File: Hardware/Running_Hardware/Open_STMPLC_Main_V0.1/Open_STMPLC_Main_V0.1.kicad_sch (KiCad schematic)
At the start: 0 parts

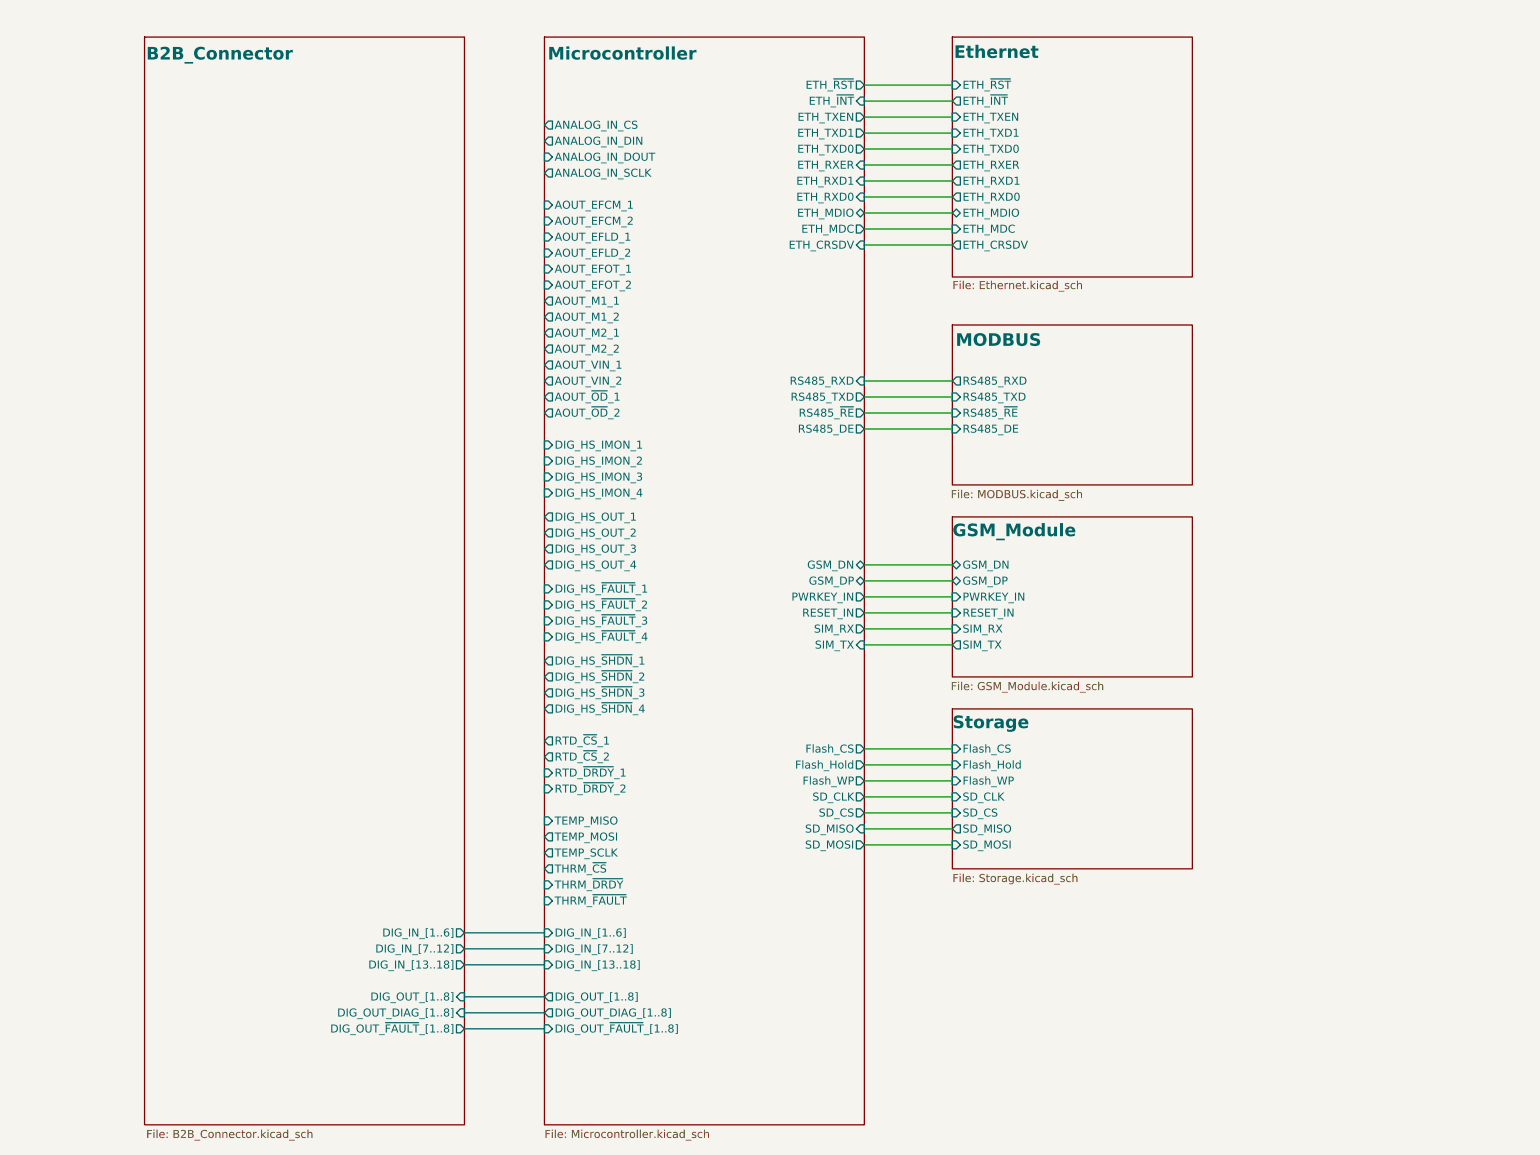
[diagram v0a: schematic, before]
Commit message: Pin mapping IO connector
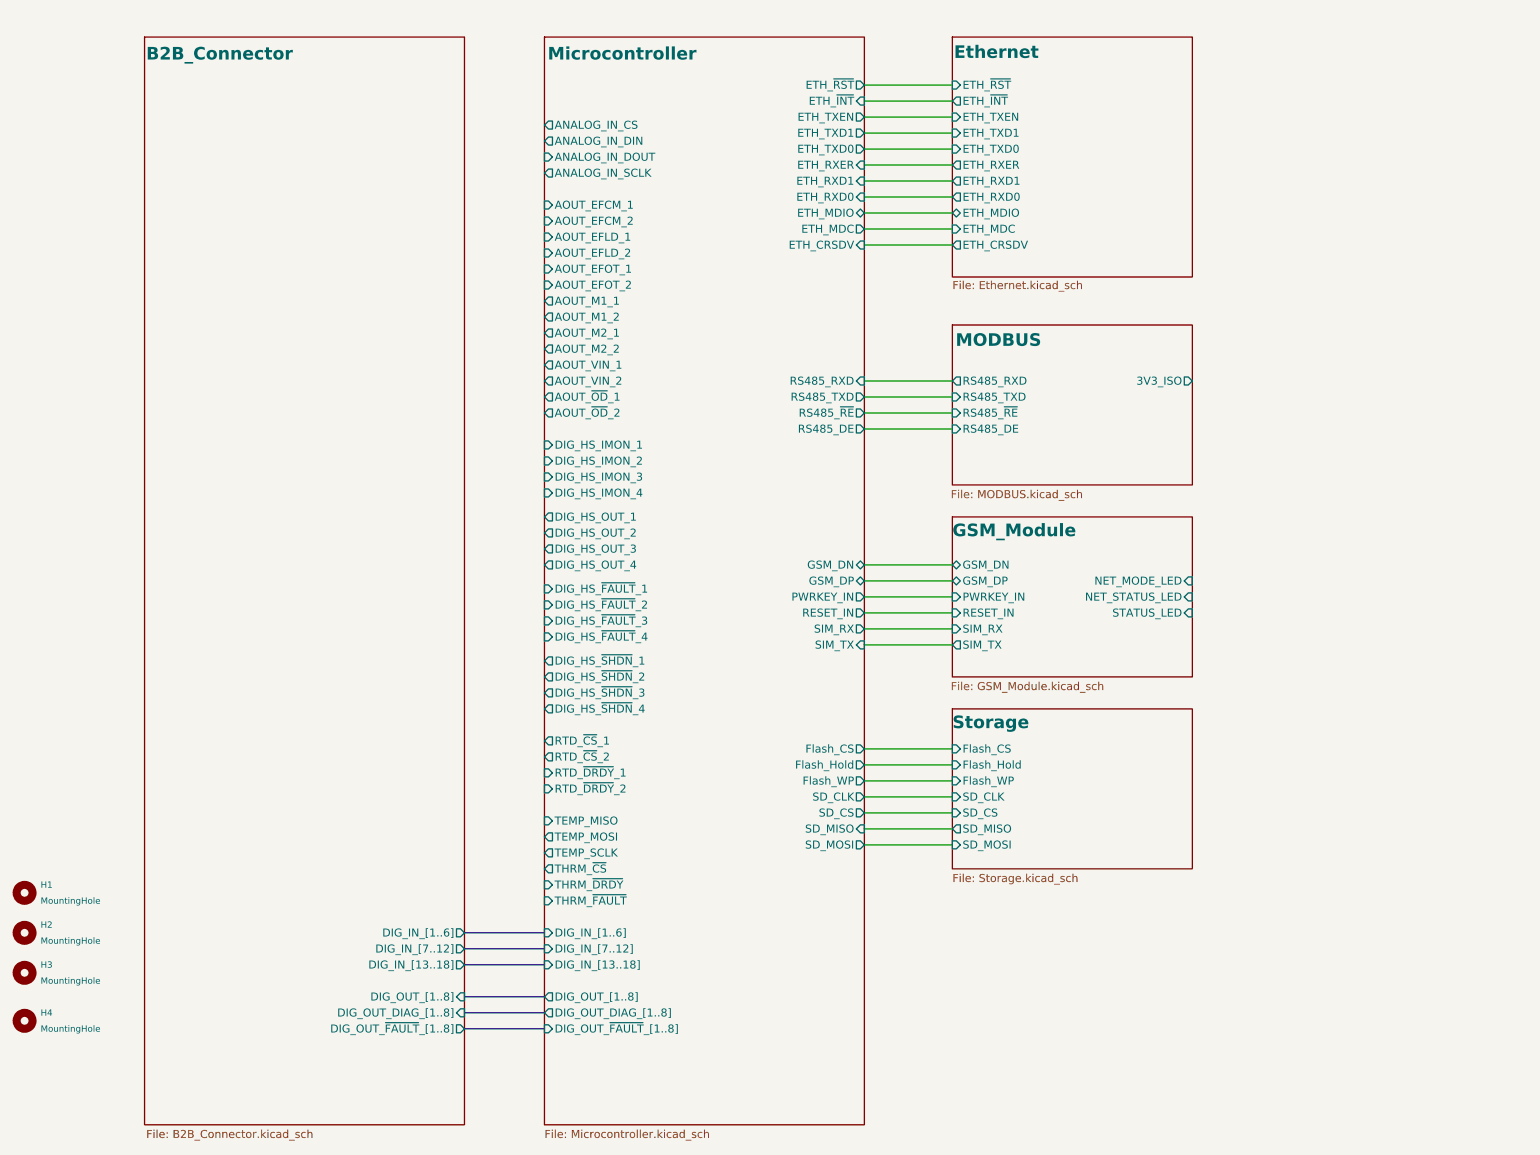
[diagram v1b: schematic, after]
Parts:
- added H1, H2, H3, H4: MountingHole, MountingHole:MountingHole_3.2mm_M3, symbol Mechanical:MountingHole
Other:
- sheet GSM_Module ports: added NET_MODE_LED, NET_STATUS_LED, STATUS_LED; removed none
- sheet MODBUS ports: added 3V3_ISO; removed none

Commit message: Main PCB changes
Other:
- sheet B2B_Connector ports: added 3V3_ISO, AB+, AB-, ANALOG_IN_CS, ANALOG_IN_DIN, ANALOG_IN_DOUT, ANALOG_IN_ERROR, ANALOG_IN_SCLK, AOUT_EFCM_1, AOUT_EFCM_2, AOUT_EFLD_1, AOUT_EFLD_2, AOUT_EFOT_1, AOUT_EFOT_2, AOUT_M1_1, AOUT_M1_2, AOUT_M2_1, AOUT_M2_2, AOUT_VIN_1, AOUT_VIN_2, AOUT_~{OD}_1, AOUT_~{OD}_2, DIG_HS_IMON_1, DIG_HS_IMON_2, DIG_HS_IMON_3, DIG_HS_IMON_4, DIG_HS_OUT_1, DIG_HS_OUT_2, DIG_HS_OUT_3, DIG_HS_OUT_4, DIG_HS_~{FAULT}_1, DIG_HS_~{FAULT}_2, DIG_HS_~{FAULT}_3, DIG_HS_~{FAULT}_4, DIG_HS_~{SHDN}_1, DIG_HS_~{SHDN}_2, DIG_HS_~{SHDN}_3, DIG_HS_~{SHDN}_4, GSM_STATUS_LED, NET_MODE_LED, NET_STATUS_LED, RTD_~{CS}_1, RTD_~{CS}_2, RTD_~{DRDY}_1, RTD_~{DRDY}_2, TEMP_MISO, TEMP_MOSI, TEMP_SCLK, THRM_~{CS}, THRM_~{DRDY}, THRM_~{FAULT}, YZ+, YZ-; removed none
- sheet GSM_Module ports: added GSM_STATUS_LED; removed STATUS_LED
- sheet MODBUS ports: added AB+, AB-, YZ+, YZ-; removed none
- sheet Microcontroller ports: added ANALOG_IN_ERROR; removed none
- moved on the sheet: H1, H2, H3, H4

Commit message: Component placement main pcb
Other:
- sheet Ethernet ports: added ETH_REFCLKO; removed ETH_~{INT}
- sheet Microcontroller ports: added ETH_REFCLKO, Flash_CLK, Flash_MISO, Flash_MOSI, SD_CMD, SD_DAT0, SD_DAT1, SD_DAT2, SD_DAT3, SD_DET; removed ETH_~{INT}, SD_CS, SD_MISO, SD_MOSI
- sheet Storage ports: added Flash_CLK, Flash_MISO, Flash_MOSI, SD_CMD, SD_DAT0, SD_DAT1, SD_DAT2, SD_DAT3, SD_DET; removed SD_CS, SD_MISO, SD_MOSI

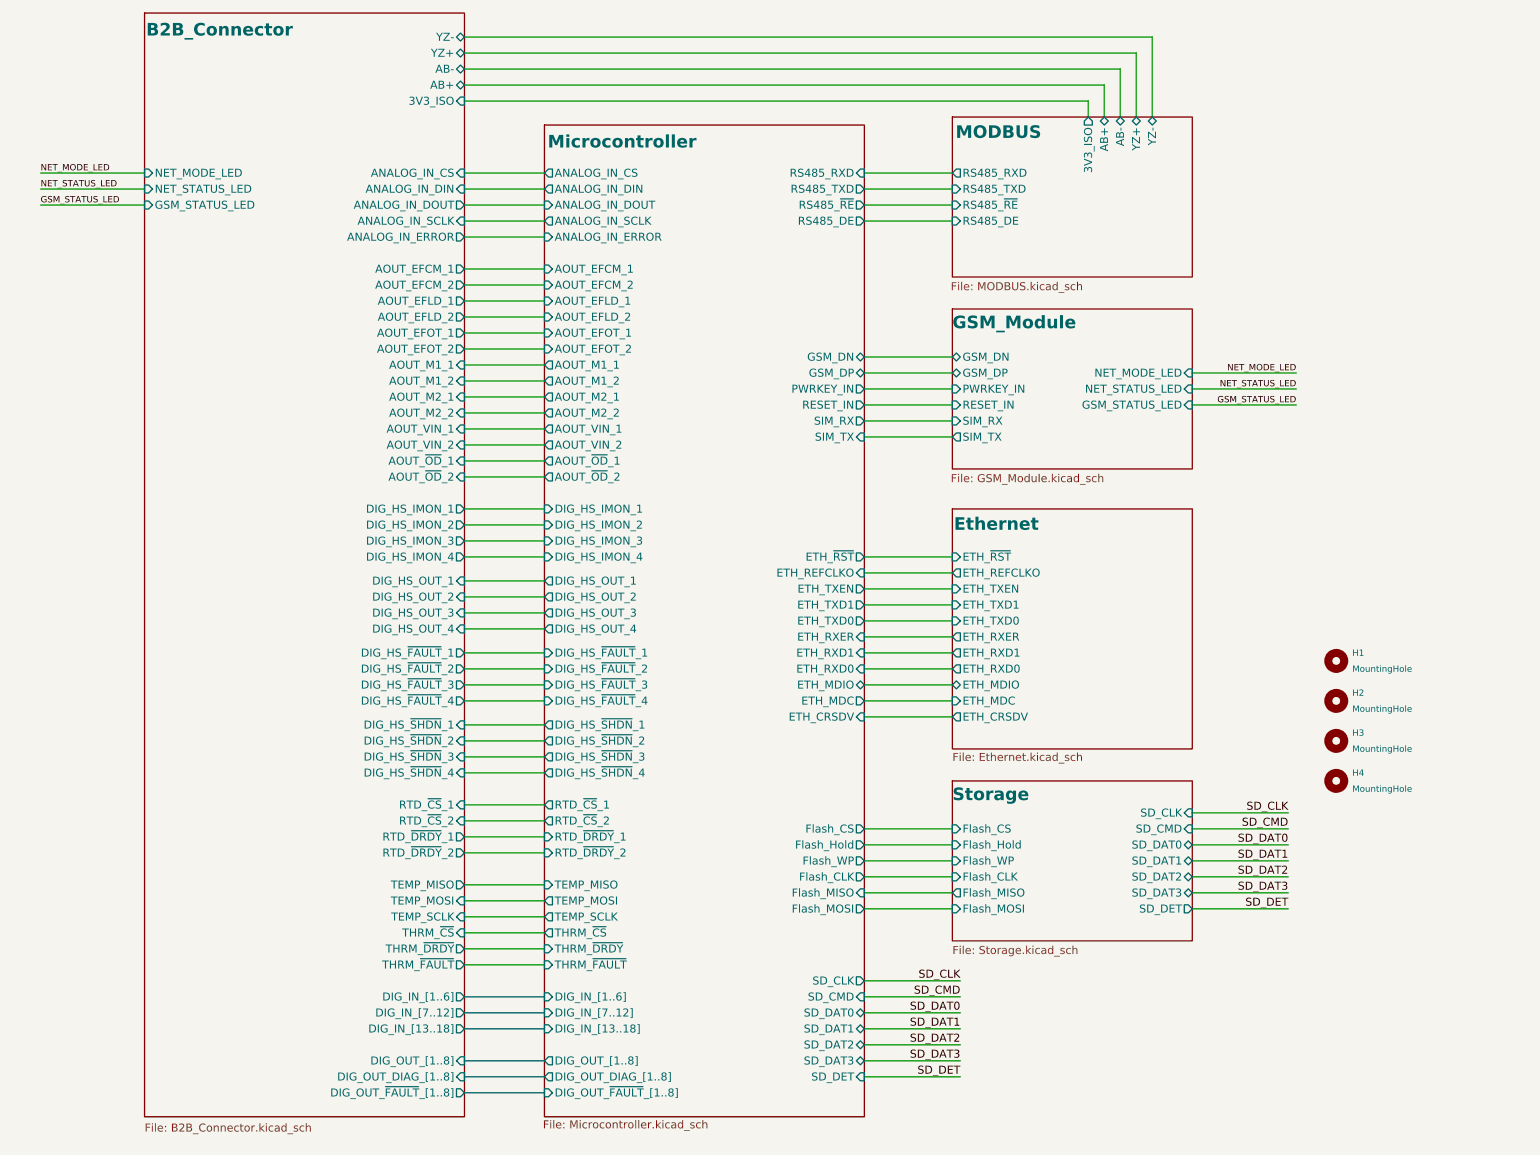
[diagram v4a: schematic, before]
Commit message: Layer stack up main PCB and pin mapping
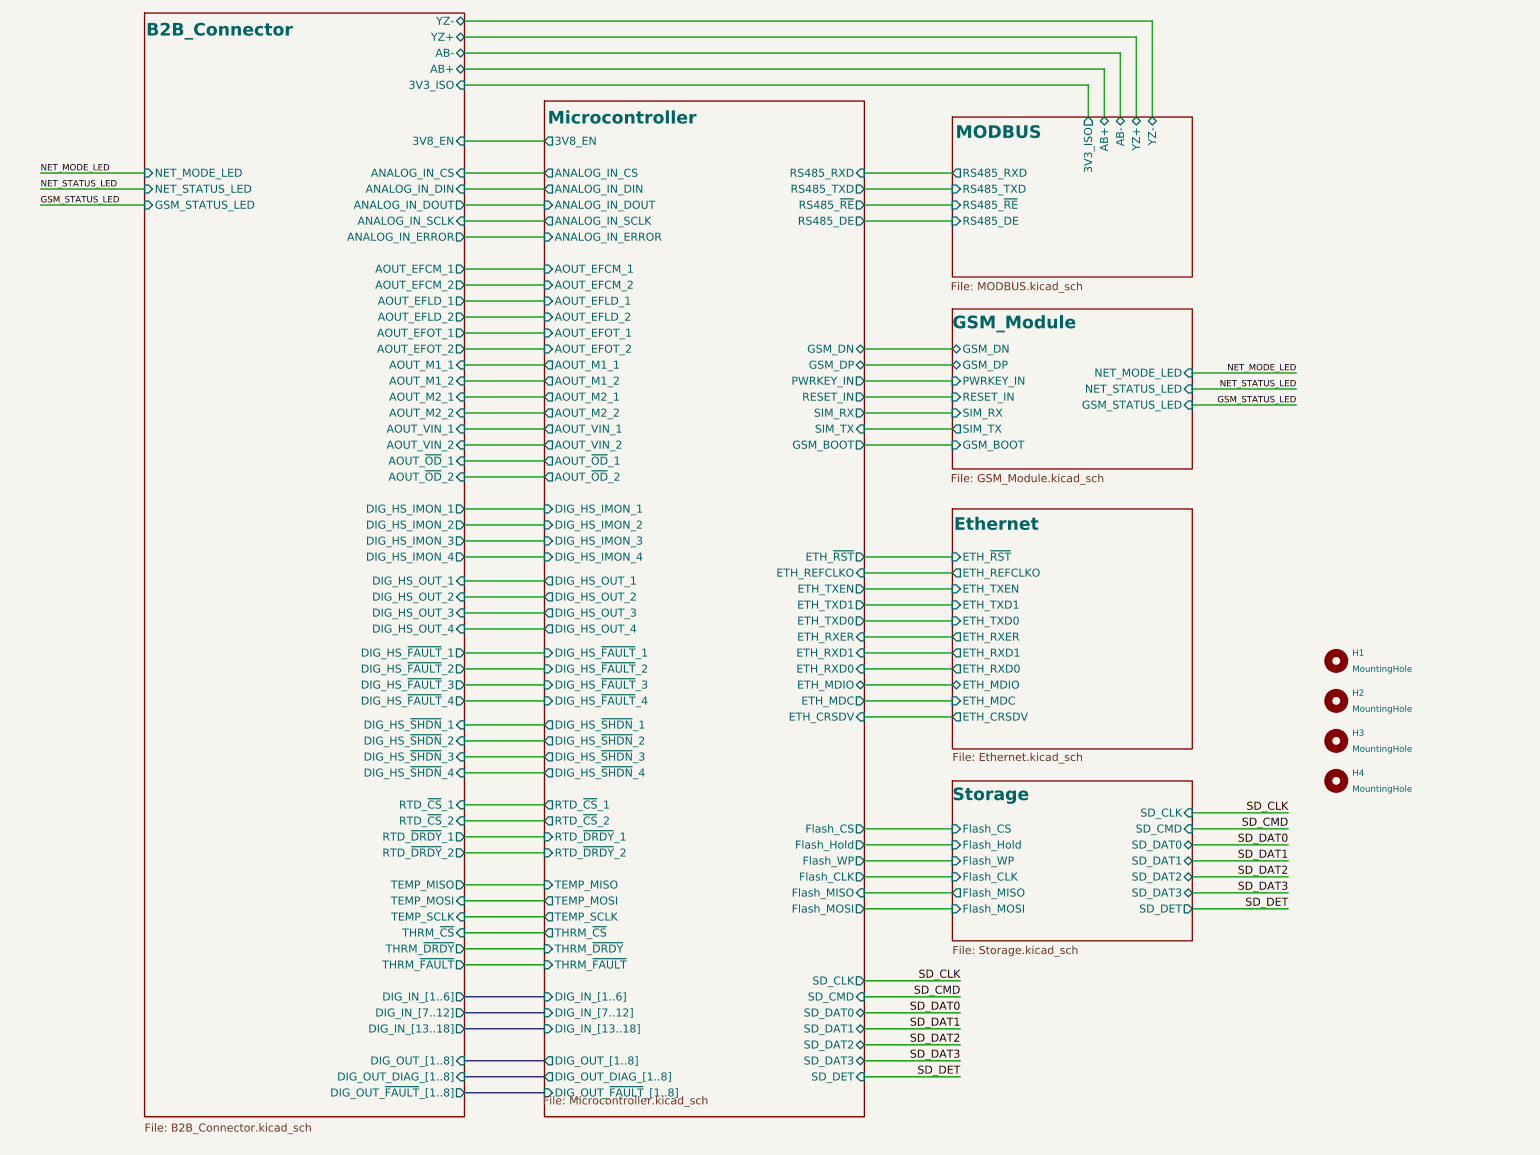
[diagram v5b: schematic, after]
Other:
- sheet B2B_Connector ports: added 3V8_EN; removed none
- sheet GSM_Module ports: added GSM_BOOT; removed none
- sheet Microcontroller ports: added 3V8_EN, GSM_BOOT; removed none
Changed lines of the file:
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@@
 	(wire
 		(pts
+			(xy 95.25 34.29) (xy 107.95 34.29)
+		)
+		(stroke
+			(width 0)
+			(type default)
+		)
+	)
+	(wire
+		(pts
 			(xy 95.25 157.48) (xy 107.95 157.48)
 		)
@@
 	(wire
 		(pts
-			(xy 158.75 68.58) (xy 172.72 68.58)
+			(xy 158.75 67.31) (xy 172.72 67.31)
 		)
 		(stroke
@@
 	(wire
 		(pts
-			(xy 196.85 30.48) (xy 196.85 25.4)
+			(xy 196.85 30.48) (xy 196.85 22.86)
 		)
 		(stroke
@@
 	(wire
 		(pts
-			(xy 201.93 20.32) (xy 201.93 30.48)
+			(xy 201.93 17.78) (xy 201.93 30.48)
 		)
 		(stroke
@@
 	(wire
 		(pts
-			(xy 204.47 30.48) (xy 204.47 17.78)
+			(xy 204.47 30.48) (xy 204.47 15.24)
 		)
 		(stroke
@@
 	(wire
 		(pts
-			(xy 194.31 27.94) (xy 194.31 30.48)
+			(xy 194.31 25.4) (xy 194.31 30.48)
 		)
 		(stroke
@@
 	(wire
 		(pts
+			(xy 158.75 82.55) (xy 172.72 82.55)
+		)
+		(stroke
+			(width 0)
+			(type default)
+		)
+	)
+	(wire
+		(pts
 			(xy 95.25 132.08) (xy 107.95 132.08)
 		)
@@
 	(wire
 		(pts
-			(xy 158.75 78.74) (xy 172.72 78.74)
+			(xy 158.75 77.47) (xy 172.72 77.47)
 		)
 		(stroke
@@
 	(wire
 		(pts
-			(xy 95.25 20.32) (xy 201.93 20.32)
+			(xy 95.25 17.78) (xy 201.93 17.78)
 		)
 		(stroke
@@
 	(wire
 		(pts
-			(xy 95.25 17.78) (xy 204.47 17.78)
+			(xy 95.25 15.24) (xy 204.47 15.24)
 		)
 		(stroke
@@
 	(wire
 		(pts
-			(xy 158.75 71.12) (xy 172.72 71.12)
+			(xy 158.75 69.85) (xy 172.72 69.85)
 		)
 		(stroke
@@
 	(wire
 		(pts
-			(xy 158.75 73.66) (xy 172.72 73.66)
+			(xy 158.75 72.39) (xy 172.72 72.39)
 		)
 		(stroke
@@
 	(wire
 		(pts
-			(xy 158.75 81.28) (xy 172.72 81.28)
+			(xy 158.75 80.01) (xy 172.72 80.01)
 		)
 		(stroke
@@
 	(wire
 		(pts
-			(xy 196.85 25.4) (xy 95.25 25.4)
+			(xy 196.85 22.86) (xy 95.25 22.86)
 		)
 		(stroke
@@
 	(wire
 		(pts
-			(xy 199.39 30.48) (xy 199.39 22.86)
+			(xy 199.39 30.48) (xy 199.39 20.32)
 		)
 		(stroke
@@
 	(wire
 		(pts
-			(xy 95.25 22.86) (xy 199.39 22.86)
+			(xy 95.25 20.32) (xy 199.39 20.32)
 		)
 		(stroke
@@
 	(wire
 		(pts
-			(xy 158.75 76.2) (xy 172.72 76.2)
+			(xy 158.75 74.93) (xy 172.72 74.93)
 		)
 		(stroke
@@
 	(wire
 		(pts
-			(xy 95.25 27.94) (xy 194.31 27.94)
+			(xy 95.25 25.4) (xy 194.31 25.4)
 		)
 		(stroke
@@
 		)
 		(pin "3V3_ISO" input
-			(at 95.25 27.94 0)
+			(at 95.25 25.4 0)
 			(effects
 				(font
@@
 		)
 		(pin "AB+" bidirectional
-			(at 95.25 25.4 0)
+			(at 95.25 22.86 0)
 			(effects
 				(font
@@
 		)
 		(pin "AB-" bidirectional
-			(at 95.25 22.86 0)
+			(at 95.25 20.32 0)
 			(effects
 				(font
@@
 		)
 		(pin "YZ+" bidirectional
-			(at 95.25 20.32 0)
+			(at 95.25 17.78 0)
 			(effects
 				(font
@@
 		)
 		(pin "YZ-" bidirectional
-			(at 95.25 17.78 0)
+			(at 95.25 15.24 0)
 			(effects
 				(font
@@
 			)
 		)
+		(pin "3V8_EN" input
+			(at 95.25 34.29 0)
+			(effects
+				(font
+					(size 1.27 1.27)
+				)
+				(justify right)
+			)
+		)
 		(instances
 			(project "Open_STMPLC_Main_V0.1"
@@
 	)
 	(sheet
-		(at 107.95 31.75)
-		(size 50.8 157.48)
+		(at 107.95 27.94)
+		(size 50.8 161.29)
 		(exclude_from_sim no)
 		(in_bom yes)
@@
 		)
 		(property "Sheetname" "Microcontroller"
-			(at 108.458 35.56 0)
+			(at 108.458 31.75 0)
 			(effects
 				(font
@@
 		)
 		(property "Sheetfile" "Microcontroller.kicad_sch"
-			(at 107.696 189.738 0)
+			(at 107.696 185.928 0)
 			(effects
 				(font
@@
 		)
 		(pin "GSM_DN" bidirectional
-			(at 158.75 68.58 0)
+			(at 158.75 67.31 0)
 			(effects
 				(font
@@
 		)
 		(pin "GSM_DP" bidirectional
-			(at 158.75 71.12 0)
+			(at 158.75 69.85 0)
 			(effects
 				(font
@@
 		)
 		(pin "PWRKEY_IN" output
-			(at 158.75 73.66 0)
+			(at 158.75 72.39 0)
 			(effects
 				(font
@@
 		)
 		(pin "RESET_IN" output
-			(at 158.75 76.2 0)
+			(at 158.75 74.93 0)
 			(effects
 				(font
@@
 		)
 		(pin "SIM_RX" output
-			(at 158.75 78.74 0)
+			(at 158.75 77.47 0)
 			(effects
 				(font
@@
 		)
 		(pin "SIM_TX" input
-			(at 158.75 81.28 0)
+			(at 158.75 80.01 0)
 			(effects
 				(font
@@
 			)
 		)
+		(pin "3V8_EN" output
+			(at 107.95 34.29 180)
+			(effects
+				(font
+					(size 1.27 1.27)
+				)
+				(justify left)
+			)
+		)
+		(pin "GSM_BOOT" output
+			(at 158.75 82.55 0)
+			(effects
+				(font
+					(size 1.27 1.27)
+				)
+				(justify right)
+			)
+		)
 		(instances
 			(project "Open_STMPLC_Main_V0.1"
@@
 		)
 		(pin "GSM_DN" bidirectional
-			(at 172.72 68.58 180)
+			(at 172.72 67.31 180)
 			(effects
 				(font
@@
 		)
 		(pin "GSM_DP" bidirectional
-			(at 172.72 71.12 180)
+			(at 172.72 69.85 180)
 			(effects
 				(font
@@
 		)
 		(pin "PWRKEY_IN" input
-			(at 172.72 73.66 180)
+			(at 172.72 72.39 180)
 			(effects
 				(font
@@
 		)
 		(pin "RESET_IN" input
-			(at 172.72 76.2 180)
+			(at 172.72 74.93 180)
 			(effects
 				(font
@@
 		)
 		(pin "SIM_RX" input
-			(at 172.72 78.74 180)
+			(at 172.72 77.47 180)
 			(effects
 				(font
@@
 		)
 		(pin "SIM_TX" output
-			(at 172.72 81.28 180)
+			(at 172.72 80.01 180)
 			(effects
 				(font
@@
 			)
 		)
+		(pin "GSM_BOOT" input
+			(at 172.72 82.55 180)
+			(effects
+				(font
+					(size 1.27 1.27)
+				)
+				(justify left)
+			)
+		)
